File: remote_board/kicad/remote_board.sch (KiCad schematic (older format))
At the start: 30 parts, among them U1 WeMos_D1_mini

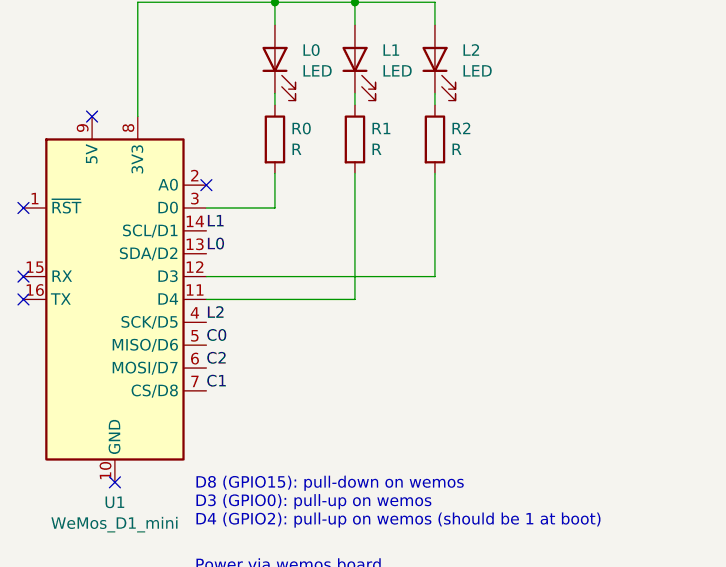
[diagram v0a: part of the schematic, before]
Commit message: Update remote kicad schematic
Fixes from prototype:
- invert C1 & L2 (D8 always measures LOW level)
- invert leds on D3/D4 (for the builtin led to be on Z)
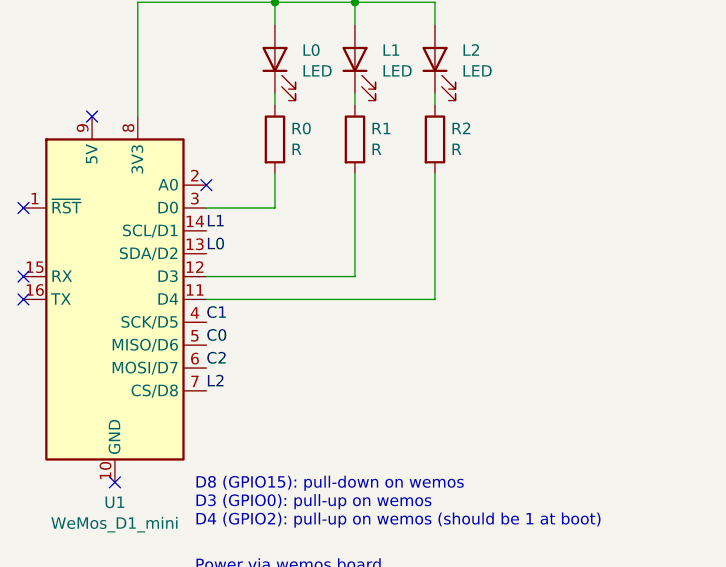
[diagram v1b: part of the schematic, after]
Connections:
- net C1: now also U1.4 (SCK/D5); no longer U1.7 (CS/D8)
- net L2: now also U1.7 (CS/D8); no longer U1.4 (SCK/D5)
- net at U1.11 (D4): now also R2.2; no longer R1.2
- net at U1.12 (D3): now also R1.2; no longer R2.2
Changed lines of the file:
@@
 Wire Wire Line
 	3700 2850 4050 2850
-Wire Wire Line
-	4050 3600 4050 4050
 $Comp
 L Switch:SW_Push S1
@@
 Text Label 3050 3850 0    50   ~ 0
 L1
-Text Label 3050 4250 0    50   ~ 0
+Text Label 3050 4550 0    50   ~ 0
 L2
 $Comp
@@
 NoConn ~ 2650 4950
 Wire Wire Line
-	3050 4150 3700 4150
-Wire Wire Line
-	3700 3600 3700 4150
-Wire Wire Line
-	3050 4050 4050 4050
+	3700 3600 3700 4050
 $Comp
 L Device:R R3
@@
 Text Label 3050 4450 0    50   ~ 0
 C2
-Text Label 3050 4550 0    50   ~ 0
+Text Label 3050 4250 0    50   ~ 0
 C1
 $Comp
@@
 Text Notes 3000 5350 0    50   ~ 0
 Power via wemos board
+Wire Wire Line
+	3050 4050 3700 4050
+Wire Wire Line
+	4050 3600 4050 4150
+Wire Wire Line
+	3050 4150 4050 4150
 $EndSCHEMATC

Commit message: Change button footprint in remote board
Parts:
- S0, S1, S2, S3, S4, S5, S6, S7, S8: footprint Button_Switch_THT:SW_PUSH_6mm -> custom_footprints:SW_PUSH_5mm_2pins
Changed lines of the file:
@@
 F 0 "S1" H 7950 3885 50  0000 C CNN
 F 1 "SW_Push" H 7950 3794 50  0000 C CNN
-F 2 "Button_Switch_THT:SW_PUSH_6mm" H 7950 3800 50  0001 C CNN
+F 2 "custom_footprints:SW_PUSH_5mm_2pins" H 7950 3800 50  0001 C CNN
 F 3 "~" H 7950 3800 50  0001 C CNN
 	1    7950 3600
@@
 F 0 "S2" H 9150 3885 50  0000 C CNN
 F 1 "SW_Push" H 9150 3794 50  0000 C CNN
-F 2 "Button_Switch_THT:SW_PUSH_6mm" H 9150 3800 50  0001 C CNN
+F 2 "custom_footprints:SW_PUSH_5mm_2pins" H 9150 3800 50  0001 C CNN
 F 3 "~" H 9150 3800 50  0001 C CNN
 	1    9150 3600
@@
 F 0 "S0" H 6700 3885 50  0000 C CNN
 F 1 "SW_Push" H 6700 3794 50  0000 C CNN
-F 2 "Button_Switch_THT:SW_PUSH_6mm" H 6700 3800 50  0001 C CNN
+F 2 "custom_footprints:SW_PUSH_5mm_2pins" H 6700 3800 50  0001 C CNN
 F 3 "~" H 6700 3800 50  0001 C CNN
 	1    6700 3600
@@
 F 0 "S4" H 7950 4485 50  0000 C CNN
 F 1 "SW_Push" H 7950 4394 50  0000 C CNN
-F 2 "Button_Switch_THT:SW_PUSH_6mm" H 7950 4400 50  0001 C CNN
+F 2 "custom_footprints:SW_PUSH_5mm_2pins" H 7950 4400 50  0001 C CNN
 F 3 "~" H 7950 4400 50  0001 C CNN
 	1    7950 4200
@@
 F 0 "S5" H 9150 4485 50  0000 C CNN
 F 1 "SW_Push" H 9150 4394 50  0000 C CNN
-F 2 "Button_Switch_THT:SW_PUSH_6mm" H 9150 4400 50  0001 C CNN
+F 2 "custom_footprints:SW_PUSH_5mm_2pins" H 9150 4400 50  0001 C CNN
 F 3 "~" H 9150 4400 50  0001 C CNN
 	1    9150 4200
@@
 F 0 "S3" H 6700 4485 50  0000 C CNN
 F 1 "SW_Push" H 6700 4394 50  0000 C CNN
-F 2 "Button_Switch_THT:SW_PUSH_6mm" H 6700 4400 50  0001 C CNN
+F 2 "custom_footprints:SW_PUSH_5mm_2pins" H 6700 4400 50  0001 C CNN
 F 3 "~" H 6700 4400 50  0001 C CNN
 	1    6700 4200
@@
 F 0 "S7" H 7950 5085 50  0000 C CNN
 F 1 "SW_Push" H 7950 4994 50  0000 C CNN
-F 2 "Button_Switch_THT:SW_PUSH_6mm" H 7950 5000 50  0001 C CNN
+F 2 "custom_footprints:SW_PUSH_5mm_2pins" H 7950 5000 50  0001 C CNN
 F 3 "~" H 7950 5000 50  0001 C CNN
 	1    7950 4800
@@
 F 0 "S8" H 9150 5085 50  0000 C CNN
 F 1 "SW_Push" H 9150 4994 50  0000 C CNN
-F 2 "Button_Switch_THT:SW_PUSH_6mm" H 9150 5000 50  0001 C CNN
+F 2 "custom_footprints:SW_PUSH_5mm_2pins" H 9150 5000 50  0001 C CNN
 F 3 "~" H 9150 5000 50  0001 C CNN
 	1    9150 4800
@@
 F 0 "S6" H 6700 5085 50  0000 C CNN
 F 1 "SW_Push" H 6700 4994 50  0000 C CNN
-F 2 "Button_Switch_THT:SW_PUSH_6mm" H 6700 5000 50  0001 C CNN
+F 2 "custom_footprints:SW_PUSH_5mm_2pins" H 6700 5000 50  0001 C CNN
 F 3 "~" H 6700 5000 50  0001 C CNN
 	1    6700 4800

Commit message: Change meaning of left/right buttons in remote board
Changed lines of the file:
@@
 C2
 Text Notes 6850 4750 0    50   ~ 0
+✗
+Text Notes 9300 4750 0    50   ~ 0
 ✓
-Text Notes 9300 4750 0    50   ~ 0
-✗
 Text Notes 8100 4750 0    50   ~ 0
 •
